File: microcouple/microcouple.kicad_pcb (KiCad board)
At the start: 2 copper layers, 124 parts, among them J1 Conn_ARM_SWD_TagConnect_TC203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, P1 USB_C_Plug, Q1 AO3415, SW1 ~{RESET}, SW2 SW_SPDT_MSK12CO2, U1 USBLC6-2SC6, U2 RP2040, U3 MCP73831-2-OT, U4 LM3671MFX, U6 IS31FL3729, U7 CAP1188, U8 TSOP34138, X1 12MHz 12pF

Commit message: Preliminary layout
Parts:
- removed U8: TSOP34138, OptoDevice:Vishay_MOLD-3Pin
- added SW3: CS1, Connector_PinHeader_2.00mm:PinHeader_1x02_P2.00mm_Vertical, F.Cu at (181.6, 87.0)
- added SW4: CS3, Connector_PinHeader_2.00mm:PinHeader_1x02_P2.00mm_Vertical, F.Cu at (181.6, 90.0)
- added SW5: CS5, Connector_PinHeader_2.00mm:PinHeader_1x02_P2.00mm_Vertical, F.Cu at (181.6, 93.0)
- added U5: IRM-V838M3-C/TR1, easyeda2kicad:OPTO-SMD_IRM-V838M3-C-TR1, F.Cu at (188.6, 104.3)
- D69: footprint LED_THT:LED_SideEmitter_Rectangular_W4.5mm_H1.6mm -> easyeda2kicad:LED-SMD_L3.0-W2.7-RD
- Q1: footprint Package_TO_SOT_SMD:SOT-23_Handsoldering -> Package_TO_SOT_SMD:SOT-23
- moved D12 97.5 mm to (185.1, 96.6), turned to 135 degrees
- moved J1 97.4 mm to (187.6, 114.5), turned to 90 degrees
- moved D11 96.0 mm to (183.5, 96.6), turned to 135 degrees
- moved D20 95.4 mm to (185.1, 98.2), turned to 135 degrees
- moved D10 94.5 mm to (181.9, 96.6), turned to 135 degrees
- moved D19 94.0 mm to (183.4, 98.2), turned to 135 degrees
- moved D28 93.8 mm to (185.1, 99.8), turned to 135 degrees
- moved D9 93.1 mm to (180.3, 96.6), turned to 135 degrees
- moved D18 92.7 mm to (181.8, 98.2), turned to 135 degrees
- moved D27 92.6 mm to (183.4, 99.8), turned to 135 degrees
- moved D36 92.2 mm to (185.1, 101.4), turned to 135 degrees
- moved D8 91.7 mm to (178.7, 96.6), turned to 135 degrees
- moved D26 91.5 mm to (181.8, 99.8), turned to 135 degrees
- moved D17 91.4 mm to (180.2, 98.2), turned to 135 degrees
- moved D35 90.7 mm to (183.4, 101.4), turned to 135 degrees
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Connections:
- U7 pad 18: unconnected-(U7-CS5-Pad18) -> /Capacitive Touch/CS5
- U7 pad 20: unconnected-(U7-CS3-Pad20) -> /Capacitive Touch/CS3
- U7 pad 22: unconnected-(U7-CS1-Pad22) -> /Capacitive Touch/CS1
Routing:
- net /LED Matrix/LEDMTX.C2: track 0.00 -> 17.9 mm, vias 0 -> 9
- net /LED Matrix/LEDMTX.C1: track 0.00 -> 17.8 mm, vias 0 -> 9
- net /LED Matrix/LEDMTX.C0: track 0.00 -> 17.5 mm, vias 0 -> 9
- net /LED Matrix/LEDMTX.C7: track 0.00 -> 16.9 mm, vias 0 -> 8
- net /LED Matrix/LEDMTX.C6: track 0.00 -> 16.9 mm, vias 0 -> 8
- net /LED Matrix/LEDMTX.C5: track 0.00 -> 16.8 mm, vias 0 -> 8
- net /LED Matrix/LEDMTX.C4: track 0.00 -> 16.8 mm, vias 0 -> 8
- net /LED Matrix/LEDMTX.C3: track 0.00 -> 16.7 mm, vias 0 -> 8
- net /LED Matrix/LEDMTX.R3: track 0.00 -> 11.4 mm
- net /LED Matrix/LEDMTX.R4: track 0.00 -> 11.4 mm
- net /LED Matrix/LEDMTX.R2: track 0.00 -> 11.4 mm
- net /LED Matrix/LEDMTX.R7: track 0.00 -> 11.4 mm
- net /LED Matrix/LEDMTX.R6: track 0.00 -> 11.4 mm
- net /LED Matrix/LEDMTX.R5: track 0.00 -> 11.4 mm
- net /LED Matrix/LEDMTX.R1: track 0.00 -> 11.4 mm
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- added copper zone on B.Cu, net GND
- added copper zone on F.Cu, net GND
- added copper zone on In1.Cu, net GND
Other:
- board outline added: 29.3 x 37.5 mm
- copper layers 2 -> 4

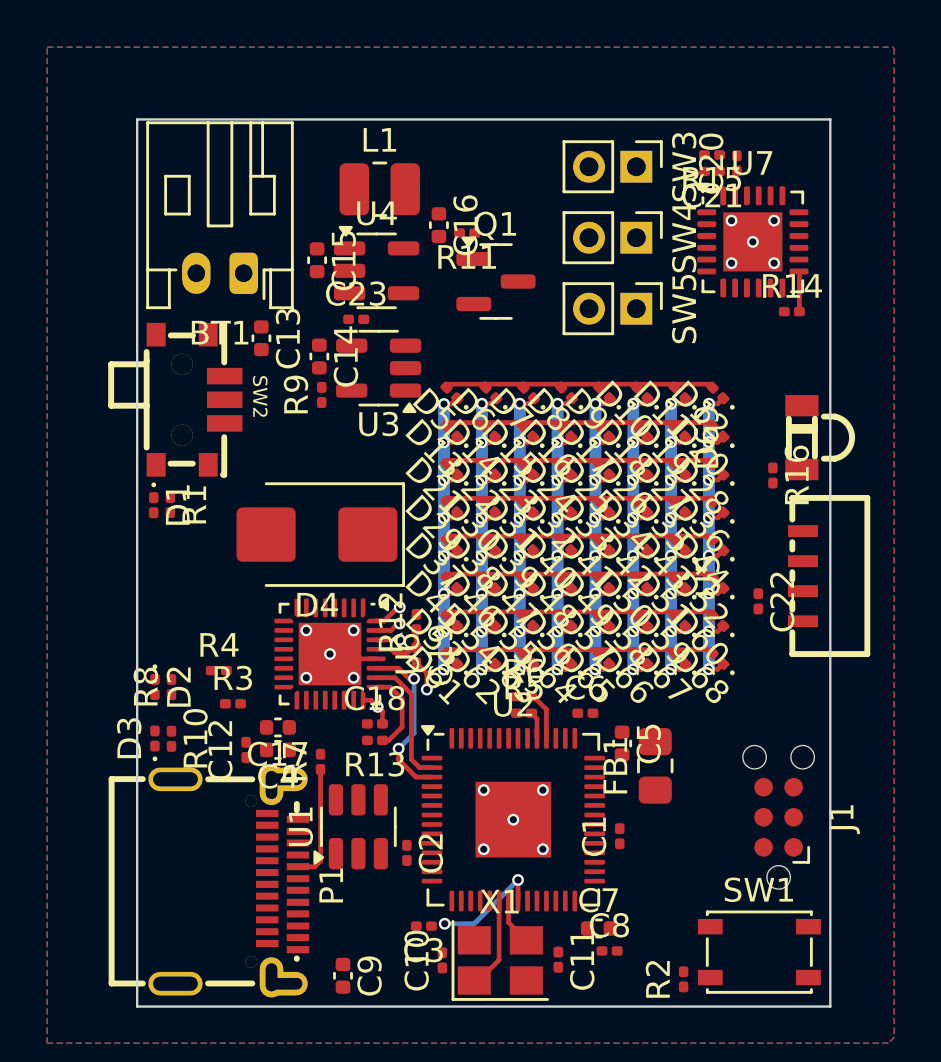
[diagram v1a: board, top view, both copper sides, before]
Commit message: Fix faulty USB-C CC pin connections
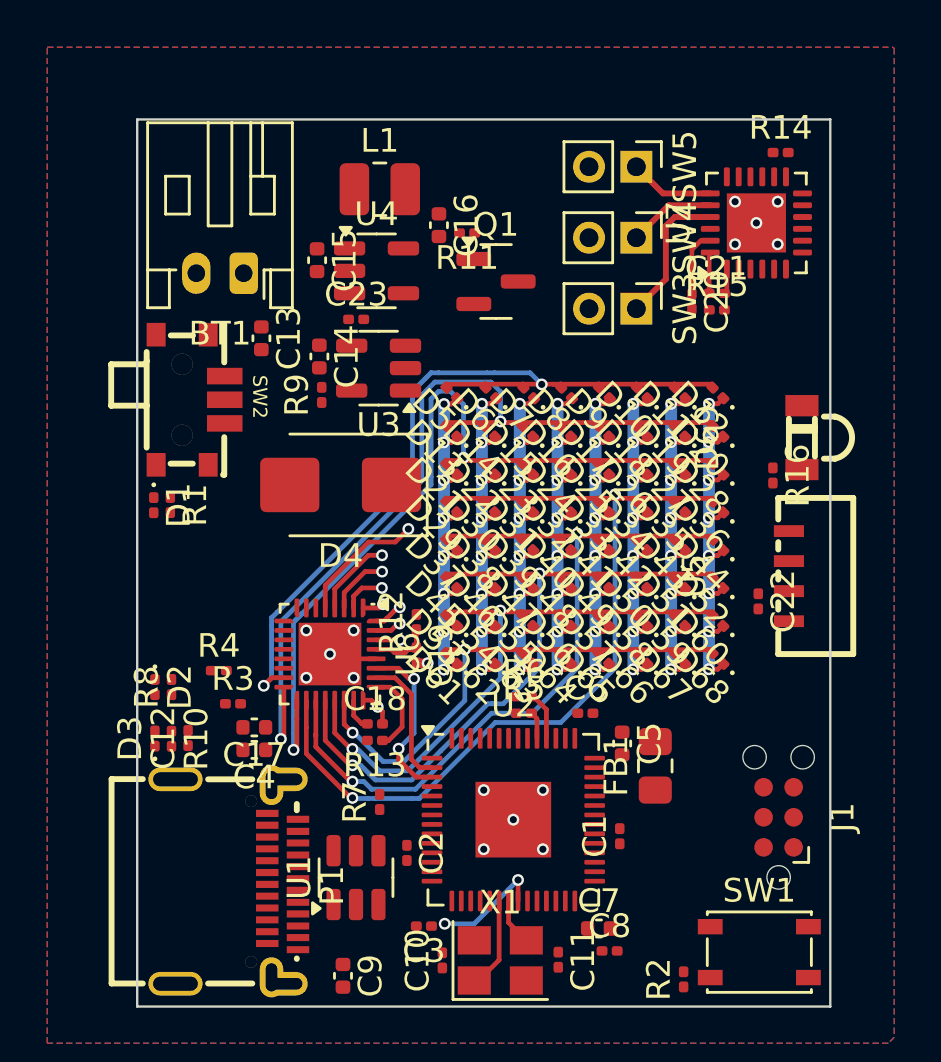
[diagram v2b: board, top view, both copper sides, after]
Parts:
- SW3: value CS1 -> CS2
- SW5: value CS5 -> CS4
- moved R14 6.74 mm to (187.7, 86.4)
- moved R15 6.55 mm to (185.0, 93.0), turned to 0 degrees
- moved C20 6.15 mm to (183.9, 92.7), turned to -90 degrees
- moved SW3 6.00 mm to (181.6, 93.0)
- moved SW5 6.00 mm to (181.6, 87.0)
- moved C21 5.15 mm to (185.0, 92.3), turned to 0 degrees
- moved R7 3.02 mm to (170.8, 113.8)
- moved C12 2.50 mm to (162.7, 111.2)
- moved D4 2.33 mm to (169.1, 100.5)
- moved U1 2.15 mm to (169.8, 117.0)
- moved C17 1.00 mm to (165.4, 110.7)
- moved C4 1.00 mm to (165.4, 111.7)
- moved U7 0.81 mm to (186.7, 89.4), turned to 90 degrees
- moved U5 0.59 mm to (188.1, 104.3)
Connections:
- SW3 pad 1: /Capacitive Touch/CS1 -> /Capacitive Touch/CS2
- SW5 pad 1: /Capacitive Touch/CS5 -> /Capacitive Touch/CS4
- U7 pad 18: /Capacitive Touch/CS5 -> unconnected-(U7-CS5-Pad18)
- U7 pad 19: unconnected-(U7-CS4-Pad19) -> /Capacitive Touch/CS4
- U7 pad 21: unconnected-(U7-CS2-Pad21) -> /Capacitive Touch/CS2
- U7 pad 22: /Capacitive Touch/CS1 -> unconnected-(U7-CS1-Pad22)
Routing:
- net /LED Matrix/LEDMTX.R4: track 11.4 -> 37.1 mm, vias 0 -> 2
- net /LED Matrix/LEDMTX.R6: track 11.4 -> 35.6 mm, vias 0 -> 2
- net /LED Matrix/LEDMTX.R5: track 11.4 -> 35.3 mm, vias 0 -> 2
- net /LED Matrix/LEDMTX.R7: track 11.4 -> 33.4 mm, vias 0 -> 2
- net /LED Matrix/LEDMTX.R3: track 11.4 -> 33.0 mm, vias 0 -> 2
- net /LED Matrix/LEDMTX.C7: track 16.9 -> 37.5 mm, vias 8 -> 9
- net /LED Matrix/LEDMTX.C6: track 16.9 -> 37.0 mm, vias 8 -> 9
- net /LED Matrix/LEDMTX.R2: track 11.4 -> 28.8 mm, vias 0 -> 2
- net /LED Matrix/LEDMTX.C5: track 16.8 -> 32.0 mm, vias 8 -> 9
- net /LED Matrix/LEDMTX.R1: track 11.4 -> 24.9 mm, vias 0 -> 2
- net /LED Matrix/LEDMTX.C4: track 16.8 -> 28.7 mm, vias 8 -> 9
- net /LED Matrix/LEDMTX.R0: track 11.4 -> 21.4 mm, vias 0 -> 2
- net /Capacitive Touch/CS2: track 0.00 -> 6.05 mm
- net /LED Matrix/LEDMTX.C2: track 17.9 -> 23.7 mm
- net Net-(P1-CC): track 4.92 -> 0.00 mm
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
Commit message: Draft layout
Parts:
- removed the C17 at (165.4, 110.7)
- removed the C9 at (169.2, 121.2)
- removed R5: 27R, Resistor_SMD:R_0201_0603Metric
- removed the R6 at (176.8, 109.4)
- removed SW3: CS2, Connector_PinHeader_2.00mm:PinHeader_1x02_P2.00mm_Vertical
- removed SW4: CS3, Connector_PinHeader_2.00mm:PinHeader_1x02_P2.00mm_Vertical
- removed SW5: CS4, Connector_PinHeader_2.00mm:PinHeader_1x02_P2.00mm_Vertical
- added C1: 4.7uF, Capacitor_SMD:C_0402_1005Metric, F.Cu at (94.5, 76.9)
- added C19: 100nF, Capacitor_SMD:C_0201_0603Metric, F.Cu at (99.8, 66.5)
- added C24: 100nF, Capacitor_SMD:C_0201_0603Metric, F.Cu at (91.1, 45.5)
- added C25: 100nF, Capacitor_SMD:C_0201_0603Metric, F.Cu at (114.8, 49.6)
- added C26: 100nF, Capacitor_SMD:C_0201_0603Metric, F.Cu at (114.8, 73.9)
- added H1: MountingHole_Pad, MountingHole:MountingHole_2.2mm_M2_DIN965_Pad, F.Cu at (88.9, 47.4)
- added H2: MountingHole_Pad, MountingHole:MountingHole_2.2mm_M2_DIN965_Pad, F.Cu at (112.9, 47.4)
- added H3: MountingHole_Pad, MountingHole:MountingHole_2.2mm_M2_DIN965_Pad, F.Cu at (112.9, 76.1)
- added J4: Conn_02x03_Odd_Even, Connector_PinHeader_1.27mm:PinHeader_2x03_P1.27mm_Vertical, F.Cu at (103.1, 48.3)
- added R2: 5.1k, Resistor_SMD:R_0201_0603Metric, F.Cu at (94.8, 71.2)
- BT1: footprint Connector_JST:JST_PH_S2B-PH-K_1x02_P2.00mm_Horizontal -> Connector_PinSocket_1.27mm:PinSocket_2x01_P1.27mm_Vertical
- J2: renamed from P1; value USB_C_Plug -> USB_C_Socket
- SW1: footprint Button_Switch_SMD:SW_SPST_PTS810 -> Button_Switch_SMD:SW_SPST_B3U-1000P
- moved R1 92.6 mm to (90.3, 68.1), turned to 0 degrees
- moved Q1 91.1 mm to (92.8, 54.0), turned to 90 degrees
- moved R9 90.9 mm to (89.5, 57.2)
- moved J1 90.5 mm to (109.7, 68.5), turned to -90 degrees
- moved C22 90.3 mm to (104.3, 50.1)
- moved SW1 90.1 mm to (109.0, 74.8), turned to -90 degrees
- moved FB1 89.6 mm to (105.8, 65.8), turned to 0 degrees
- moved U6 89.5 mm to (107.3, 48.1)
- moved R16 89.5 mm to (105.7, 51.8)
- moved C21 89.5 mm to (105.7, 51.0)
- moved C7 89.4 mm to (97.4, 70.8)
- moved R6 89.3 mm to (106.9, 75.6)
- moved C12 88.0 mm to (104.5, 75.7)
- moved D2 88.0 mm to (91.0, 60.0), turned to -135 degrees
- moved R15 87.5 mm to (110.2, 45.8), turned to -90 degrees
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- renumbered C6 to C10, C7 to C11, C8 to C12, C23 to C16, C16 to C17, C19 to C18, C12 to C2, C18 to C20, C20 to C22, C22 to C23, C10 to C3, C11 to C4, C1 to C5, C2 to C6, C3 to C7, C4 to C8, C5 to C9, D45 to D10, D53 to D11, D61 to D12, D6 to D13, D22 to D15, D30 to D16, D38 to D17, D46 to D18, D54 to D19, D4 to D2, D62 to D20, D7 to D21, D15 to D22, D31 to D24, D39 to D25, D47 to D26, D55 to D27, D63 to D28, D8 to D29, D2 to D3, D16 to D30, D24 to D31, D40 to D33, D48 to D34, D56 to D35, D64 to D36, D9 to D37, D17 to D38, D25 to D39, D3 to D4, D33 to D40, D49 to D42, D57 to D43, D65 to D44, D10 to D45, D18 to D46, D26 to D47, D34 to D48, D42 to D49, D58 to D51, D66 to D52, D11 to D53, D19 to D54, D27 to D55, D35 to D56, D43 to D57, D51 to D58, D13 to D6, D67 to D60, D12 to D61, D20 to D62, D28 to D63, D36 to D64, D44 to D65, D52 to D66, D60 to D67, D21 to D7, D29 to D8, D37 to D9, R7 to R1, R9 to R10, R8 to R11, R10 to R12, R12 to R14, R14 to R15, R15 to R16, R16 to R17, R1 to R3, R2 to R6, R3 to R7, R4 to R8, R11 to R9, U6 to U5, U7 to U6, U5 to U7
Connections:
- J2 pad A5: Net-(P1-CC) -> Net-(J2-CC1)
- J2 pad B5: unconnected-(P1-VCONN-PadB5) -> Net-(J2-CC2)
- R1 pad 1: Net-(P1-CC) -> Net-(J2-CC2)
- U2 pad 46: Net-(U2-USB_DM) -> /USB.D_PROTECTED-
- U2 pad 47: Net-(U2-USB_DP) -> /USB.D_PROTECTED+
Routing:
- net GND: track 5.13 -> 58.2 mm, vias 17 -> 51
- net /I2C0.SDL: track 7.20 -> 54.9 mm, vias 2 -> 3
- net VBUS: track 0.00 -> 36.1 mm, vias 0 -> 8
- net /I2C0.SDA: track 5.55 -> 41.2 mm, vias 0 -> 2
- net /~{CT_ALERT}: track 0.00 -> 34.8 mm, vias 0 -> 2
- net /Battery Management/Charge Status: track 0.00 -> 30.2 mm, vias 0 -> 2
- net +3.3V: track 8.94 -> 37.6 mm, vias 2 -> 14
- net /CT_RESET: track 1.74 -> 30.4 mm, vias 0 -> 2
- net /CT_WAKE: track 0.00 -> 28.2 mm, vias 0 -> 2
- net /~{MX_SDB}: track 2.61 -> 29.9 mm, vias 0 -> 2
- net /IR.TX: track 0.00 -> 21.2 mm, vias 0 -> 2
- net /USB.D+: track 0.00 -> 20.7 mm, vias 0 -> 3
- net /USB.D-: track 0.00 -> 20.7 mm, vias 0 -> 3
- net Net-(J2-SHIELD): track 0.00 -> 18.9 mm
- net /SWDIO: track 0.00 -> 15.3 mm, vias 0 -> 2
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- added copper zone on F.Cu, net +3.3V
- added copper zone on In2.Cu, net +3.3V
- added copper zone on F.Cu, net /Battery Management/VIN
- added copper zone on F.Cu, net VBUS
- added copper zone on In2.Cu, net VBUS
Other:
- board size 29.3 x 37.5 mm -> 29.5 x 34.2 mm

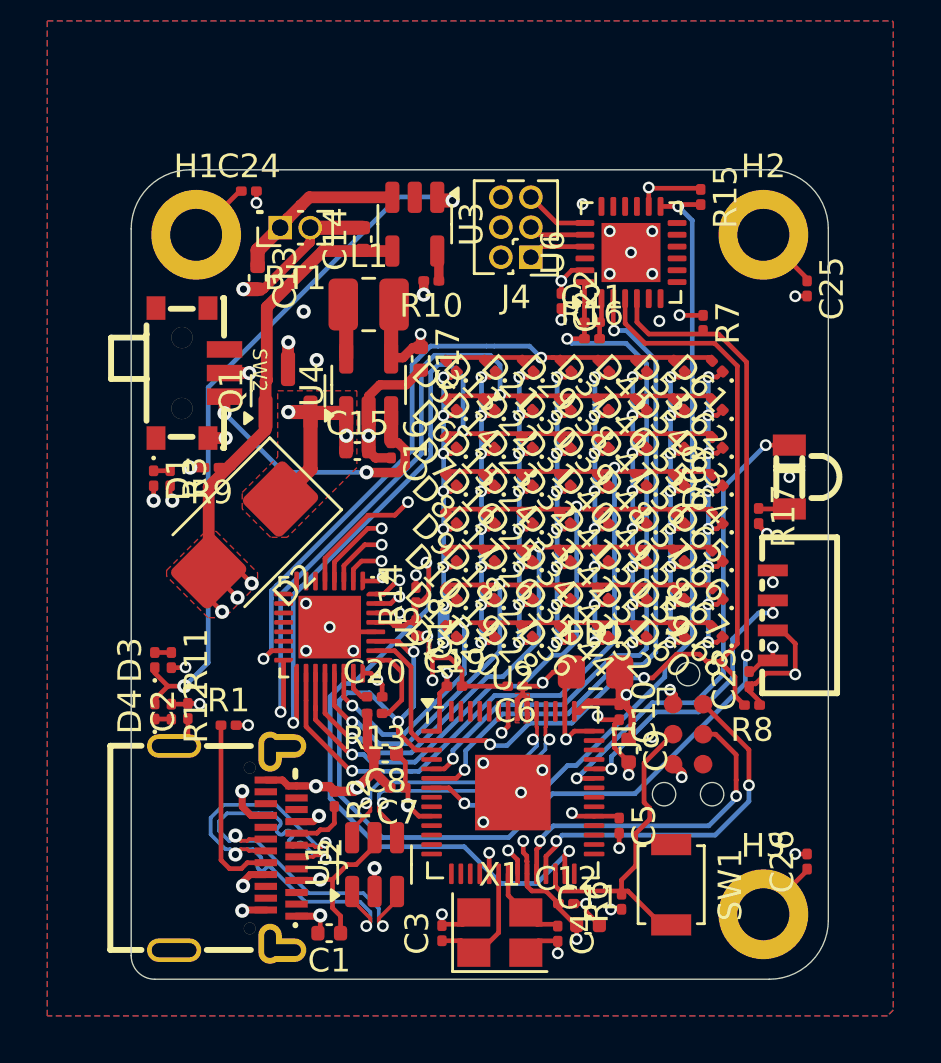
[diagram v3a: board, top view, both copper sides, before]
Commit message: Finish Silkscreen
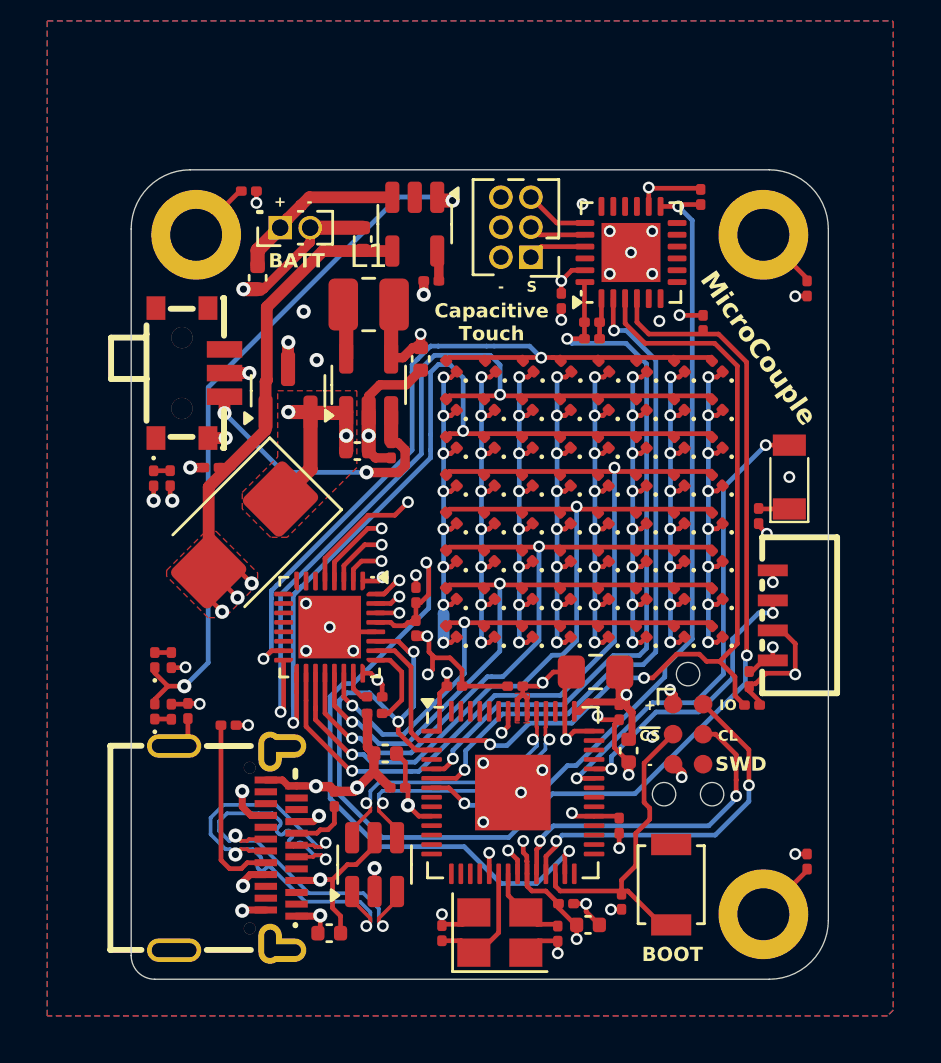
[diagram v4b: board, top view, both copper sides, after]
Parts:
- added G***: LOGO, LOGO, B.Cu at (99.3, 69.8)
- added G***: LOGO, LOGO, B.Cu at (97.3, 60.8)
- C1, C11, C13, C14, C15, C17, C8, C9: footprint Capacitor_SMD:C_0402_1005Metric -> GS_SMD:0402_1005Metric
- C10, C12, C16, C18, C19, C2, C20, C21, C22, C23, C24, C25, C26, C3, C4, C5, C6, C7: footprint Capacitor_SMD:C_0201_0603Metric -> GS_SMD:0201_0603Metric
- D1, D10, D11, D12, D13, D14, D15, D16, D17, D18, D19, D20, D21, D22, D23, D24, D25, D26, D27, D28, D29, D3, D30, D31, D32, D33, D34, D35, D36, D37, D38, D39, D4, D40, D41, D42, D43, D44, D45, D46, D47, D48, D49, D5, D50, D51, D52, D53, D54, D55, D56, D57, D58, D59, D6, D60, D61, D62, D63, D64, D65, D66, D67, D68, D7, D8, D9: footprint LED_SMD:LED_0201_0603Metric -> GS_Optoelectronics:LED_0201_0603Metric
- R1, R10, R11, R12, R13, R14, R15, R16, R17, R2, R3, R6, R7, R8, R9: footprint Resistor_SMD:R_0201_0603Metric -> GS_SMD:0201_0603Metric
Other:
- board text added: "+"
- board text added: "-"
- board text added: "38kHz IR Transciever 8x8 LED matrix USB-C Connectivity LiPo charging circuitry 3 capacitive touch inputs 3.3V logic M2 mounting"
- board text added: "BATT"
- board text added: "BOOT"
- board text added: "CL"
- board text added: "Capacitive Touch"
- board text added: "Design by George Sleen"
- board text added: "IO"
- board text added: "MicroCouple"
- board text added: "Open Source Hardware"
- board text added: "RP2040 Powered"
- board text added: "S"
- board text added: "SWD"
- board text added: "~{CS}"

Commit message: Finish layout
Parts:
- moved C20 1.09 mm to (96.2, 68.0), turned to -90 degrees
- moved R13 0.53 mm to (96.8, 68.0), turned to -90 degrees
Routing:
- net /LED Matrix/LEDMTX.C3: track 17.6 -> 27.8 mm
- net GND: track 58.1 -> 54.0 mm, vias 51 -> 52
- net +1V1: track 11.8 -> 14.9 mm
- net VBUS: track 36.1 -> 33.2 mm
- net /LED Matrix/LEDMTX.C6: track 37.0 -> 35.4 mm
- net /LED Matrix/LEDMTX.C7: track 37.5 -> 36.3 mm
- net /IR.TX: track 21.2 -> 20.2 mm
- net Net-(J2-SHIELD): track 18.9 -> 18.2 mm
- net /~{RESET}: track 14.0 -> 13.4 mm
- net /LED Matrix/LEDMTX.C5: track 32.0 -> 31.4 mm
- net +3.3VA: track 8.58 -> 8.11 mm, vias 1 -> 0
- net /Battery Management/VIN: vias 3 -> 2
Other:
- board text added: "38kHz IR Transciever 8x8 LED matrix 3 capacitive touch inputs USB-C Connectivity LiPo charging circuitry 3.3V logic M2 mounting"
- board text removed: "38kHz IR Transciever 8x8 LED matrix USB-C Connectivity LiPo charging circuitry 3 capacitive touch inputs 3.3V logic M2 mounting"
